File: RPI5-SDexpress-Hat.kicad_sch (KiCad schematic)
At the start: 51 parts, among them J1 Conn_01x16_Shielded, J11 10102166A812A, J2 Conn_01x04_Shielded, J3 Conn_01x04_Shielded, J5 Conn_02x03_Odd_Even, SW1 SW_Push, U2 STM8S003F3P, U3 LP5907MFX-3.3, U4 TCA9406DC, U5 PAM2306AYPKE

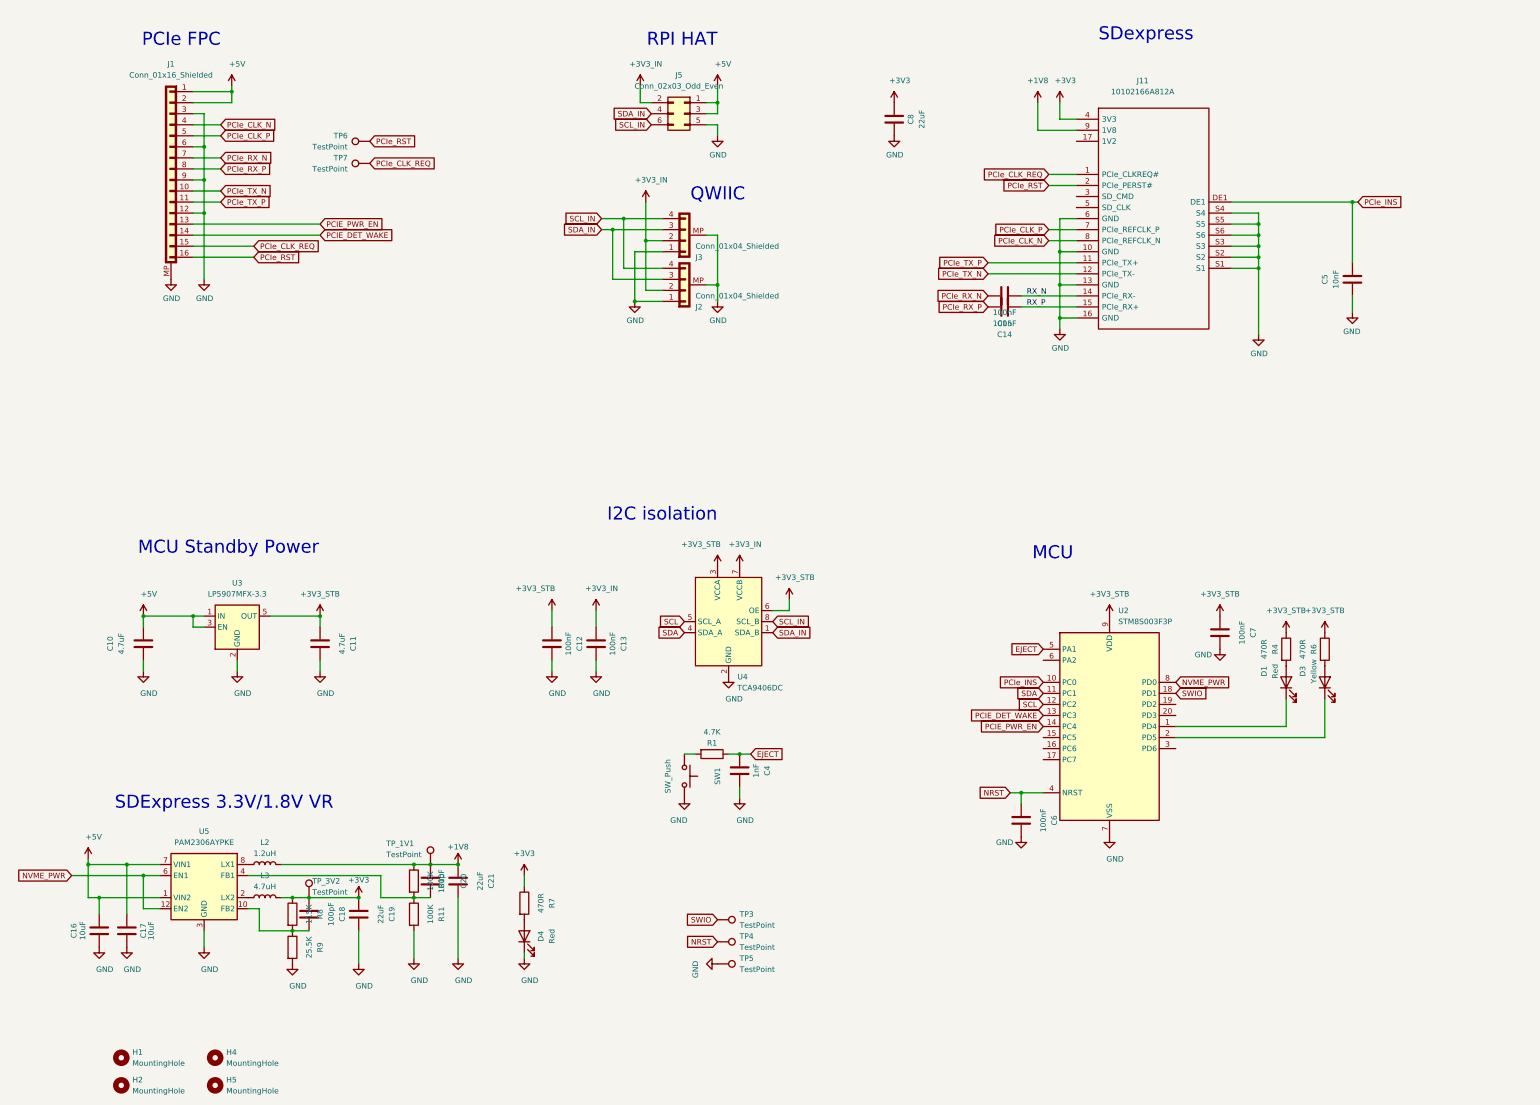
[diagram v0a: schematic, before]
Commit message: Adding BOM, clean up SCH, update FPC connector BOM
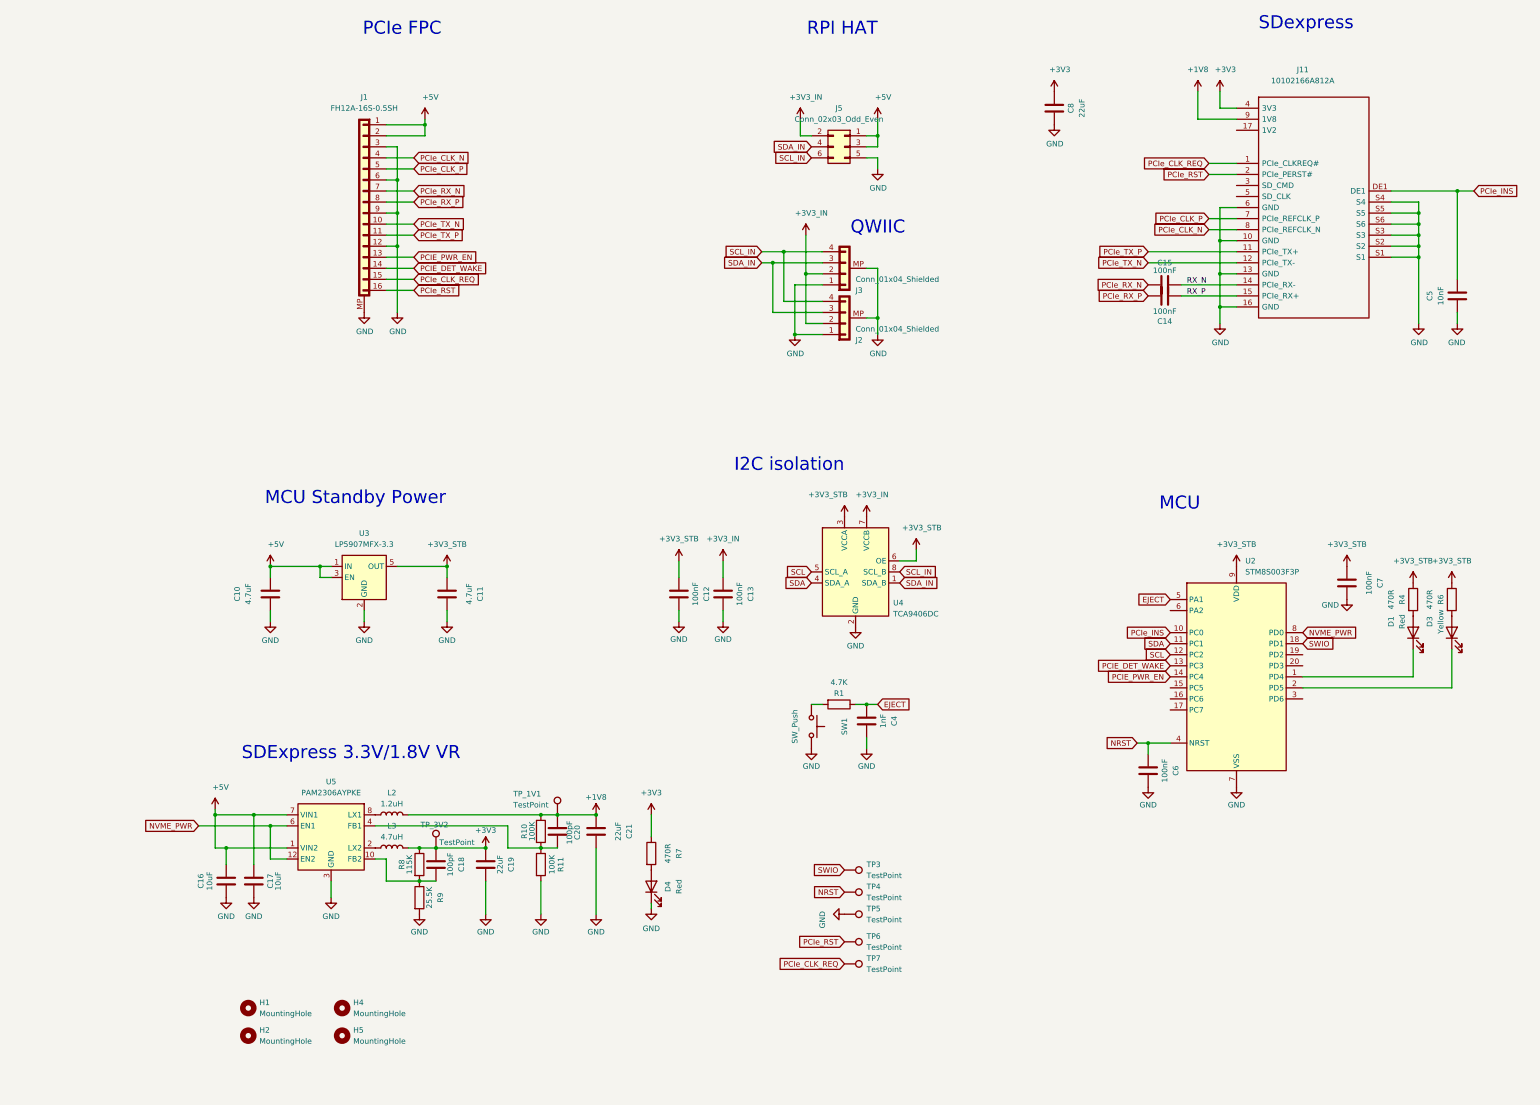
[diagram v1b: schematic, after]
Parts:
- J1: value Conn_01x16_Shielded -> FH12A-16S-0.5SH
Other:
- moved on the sheet: C10, C11, C12, C13, C14, C15, C16, C17, C18, C19, C20, C21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
